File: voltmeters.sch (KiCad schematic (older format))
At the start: 27 parts

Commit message: - added DC/DC converter to library, - moved ammeter & drivers to sub-sheet, - further develop
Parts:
- R?: value 10M -> 500M
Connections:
- net U_Wh renamed U_Ext
- net U_adcWh renamed U_adcExt
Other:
- note added: "I_drawn = U_meas/R_in"
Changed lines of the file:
@@
 $Descr A4 11693 8268
 encoding utf-8
-Sheet 7 7
+Sheet 7 8
 Title ""
 Date ""
@@
 AR Path="/5F479892/5F479BF7" Ref="R?"  Part="1"
 F 0 "R?" V 4500 2350 50  0000 C CNN
-F 1 "10M" V 4300 2350 50  0000 C CNN
+F 1 "500M" V 4300 2350 50  0000 C CNN
 F 2 "" V 4330 2350 50  0001 C CNN
 F 3 "~" H 4400 2350 50  0001 C CNN
@@
 $EndComp
 Text Notes 3350 2050 0    50   ~ 0
-I_drawn = U_meas/10M
+I_drawn = U_meas/R_in
 Wire Wire Line
 	5300 2050 5300 2350
@@
 U_K
 Text HLabel 3800 4950 0    50   Input ~ 0
-U_Wh
+U_Ext
 Text HLabel 6700 1950 2    50   Output ~ 0
 U_adcFocus
@@
 U_adcK
 Text HLabel 6700 4550 2    50   Output ~ 0
-U_adcWh
+U_adcExt
 $Comp
 L Device:C_Small C?

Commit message: - added supply sch draft
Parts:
- removed R? (x2): 10M, symbol Device:R
- added R? (x2): 500M, symbol Device:R
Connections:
- net U_Ext: now also R?.1
- net U_K: now also R?.1
- net at C?.2, R?.1, U?.2 (-): now also R?.2 (x2)
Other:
- note removed: "I_drawn = U_meas/10M"
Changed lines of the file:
@@
 $Descr A4 11693 8268
 encoding utf-8
-Sheet 7 8
+Sheet 6 9
 Title ""
 Date ""
@@
 $EndComp
 $Comp
-L power:GND #PWR?
-U 1 1 5F479BF1
-P 4700 1950
-AR Path="/5F40DCB9/5F479BF1" Ref="#PWR?"  Part="1"
-AR Path="/5F479892/5F479BF1" Ref="#PWR?"  Part="1"
-F 0 "#PWR?" H 4700 1790 50  0001 C CNN
-F 1 "GND" V 4700 1873 39  0000 R CNN
-F 2 "" H 4700 1950 50  0001 C CNN
-F 3 "" H 4700 1950 50  0001 C CNN
-	1    4700 1950
-	0    1    1    0
-$EndComp
-$Comp
 L Device:R R?
 U 1 1 5F479BF7
@@
 	1    6050 2350
 	0    -1   -1   0
-$EndComp
-$Comp
-L power:GND #PWR?
-U 1 1 5F479C10
-P 5800 1850
-AR Path="/5F40DCB9/5F479C10" Ref="#PWR?"  Part="1"
-AR Path="/5F479892/5F479C10" Ref="#PWR?"  Part="1"
-F 0 "#PWR?" H 5800 1690 50  0001 C CNN
-F 1 "GND" V 5800 1773 39  0000 R CNN
-F 2 "" H 5800 1850 50  0001 C CNN
-F 3 "" H 5800 1850 50  0001 C CNN
-	1    5800 1850
-	0    1    1    0
 $EndComp
 Wire Wire Line
@@
 	0    -1   -1   0
 $EndComp
-$Comp
-L power:GND #PWR?
-U 1 1 5F479C4C
-P 4700 3250
-AR Path="/5F40DCB9/5F479C4C" Ref="#PWR?"  Part="1"
-AR Path="/5F479892/5F479C4C" Ref="#PWR?"  Part="1"
-F 0 "#PWR?" H 4700 3090 50  0001 C CNN
-F 1 "GND" V 4700 3173 39  0000 R CNN
-F 2 "" H 4700 3250 50  0001 C CNN
-F 3 "" H 4700 3250 50  0001 C CNN
-	1    4700 3250
-	0    1    1    0
-$EndComp
-$Comp
-L Device:R R?
-U 1 1 5F479C52
-P 4400 3650
-AR Path="/5F40DCB9/5F479C52" Ref="R?"  Part="1"
-AR Path="/5F479892/5F479C52" Ref="R?"  Part="1"
-F 0 "R?" V 4500 3650 50  0000 C CNN
-F 1 "10M" V 4300 3650 50  0000 C CNN
-F 2 "" V 4330 3650 50  0001 C CNN
-F 3 "~" H 4400 3650 50  0001 C CNN
-	1    4400 3650
-	0    -1   -1   0
-$EndComp
 Wire Wire Line
 	4700 3450 4700 3650
@@
 	1    6050 3650
 	0    -1   -1   0
-$EndComp
-$Comp
-L power:GND #PWR?
-U 1 1 5F479C6B
-P 5800 3150
-AR Path="/5F40DCB9/5F479C6B" Ref="#PWR?"  Part="1"
-AR Path="/5F479892/5F479C6B" Ref="#PWR?"  Part="1"
-F 0 "#PWR?" H 5800 2990 50  0001 C CNN
-F 1 "GND" V 5800 3073 39  0000 R CNN
-F 2 "" H 5800 3150 50  0001 C CNN
-F 3 "" H 5800 3150 50  0001 C CNN
-	1    5800 3150
-	0    1    1    0
 $EndComp
 Wire Wire Line
@@
 	-1   0    0    1
 $EndComp
-Text Notes 3500 3350 0    50   ~ 0
-I_drawn = U_meas/10M
 Wire Wire Line
 	5300 3350 5300 3650
@@
 	0    -1   -1   0
 $EndComp
-$Comp
-L power:GND #PWR?
-U 1 1 5F479CA7
-P 4700 4550
-AR Path="/5F40DCB9/5F479CA7" Ref="#PWR?"  Part="1"
-AR Path="/5F479892/5F479CA7" Ref="#PWR?"  Part="1"
-F 0 "#PWR?" H 4700 4390 50  0001 C CNN
-F 1 "GND" V 4700 4473 39  0000 R CNN
-F 2 "" H 4700 4550 50  0001 C CNN
-F 3 "" H 4700 4550 50  0001 C CNN
-	1    4700 4550
-	0    1    1    0
-$EndComp
-$Comp
-L Device:R R?
-U 1 1 5F479CAD
-P 4400 4950
-AR Path="/5F40DCB9/5F479CAD" Ref="R?"  Part="1"
-AR Path="/5F479892/5F479CAD" Ref="R?"  Part="1"
-F 0 "R?" V 4500 4950 50  0000 C CNN
-F 1 "10M" V 4300 4950 50  0000 C CNN
-F 2 "" V 4330 4950 50  0001 C CNN
-F 3 "~" H 4400 4950 50  0001 C CNN
-	1    4400 4950
-	0    -1   -1   0
-$EndComp
 Wire Wire Line
 	4700 4750 4700 4950
@@
 	1    6050 4950
 	0    -1   -1   0
-$EndComp
-$Comp
-L power:GND #PWR?
-U 1 1 5F479CC6
-P 5800 4450
-AR Path="/5F40DCB9/5F479CC6" Ref="#PWR?"  Part="1"
-AR Path="/5F479892/5F479CC6" Ref="#PWR?"  Part="1"
-F 0 "#PWR?" H 5800 4290 50  0001 C CNN
-F 1 "GND" V 5800 4373 39  0000 R CNN
-F 2 "" H 5800 4450 50  0001 C CNN
-F 3 "" H 5800 4450 50  0001 C CNN
-	1    5800 4450
-	0    1    1    0
 $EndComp
 Wire Wire Line
@@
 	-1   0    0    1
 $EndComp
-Text Notes 3450 4600 0    50   ~ 0
-I_drawn = U_meas/10M
 Wire Wire Line
 	5300 4650 5300 4950
@@
 Wire Wire Line
 	6400 5200 6400 4950
+$Comp
+L power:GND #PWR?
+U 1 1 5F62A73A
+P 4700 1950
+AR Path="/5F40DCB9/5F62A73A" Ref="#PWR?"  Part="1"
+AR Path="/5F618AB9/5F62A73A" Ref="#PWR?"  Part="1"
+AR Path="/5F62A73A" Ref="#PWR?"  Part="1"
+AR Path="/5F479892/5F62A73A" Ref="#PWR?"  Part="1"
+F 0 "#PWR?" H 4700 1790 50  0001 C CNN
+F 1 "GND" V 4700 1850 39  0000 R CNN
+F 2 "" H 4700 1950 50  0001 C CNN
+F 3 "" H 4700 1950 50  0001 C CNN
+	1    4700 1950
+	0    1    1    0
+$EndComp
+$Comp
+L power:GND #PWR?
+U 1 1 5F62B7FF
+P 5800 1850
+AR Path="/5F40DCB9/5F62B7FF" Ref="#PWR?"  Part="1"
+AR Path="/5F618AB9/5F62B7FF" Ref="#PWR?"  Part="1"
+AR Path="/5F62B7FF" Ref="#PWR?"  Part="1"
+AR Path="/5F479892/5F62B7FF" Ref="#PWR?"  Part="1"
+F 0 "#PWR?" H 5800 1690 50  0001 C CNN
+F 1 "GND" V 5800 1750 39  0000 R CNN
+F 2 "" H 5800 1850 50  0001 C CNN
+F 3 "" H 5800 1850 50  0001 C CNN
+	1    5800 1850
+	0    1    1    0
+$EndComp
+$Comp
+L power:GND #PWR?
+U 1 1 5F62C9BB
+P 4700 3250
+AR Path="/5F40DCB9/5F62C9BB" Ref="#PWR?"  Part="1"
+AR Path="/5F618AB9/5F62C9BB" Ref="#PWR?"  Part="1"
+AR Path="/5F62C9BB" Ref="#PWR?"  Part="1"
+AR Path="/5F479892/5F62C9BB" Ref="#PWR?"  Part="1"
+F 0 "#PWR?" H 4700 3090 50  0001 C CNN
+F 1 "GND" V 4700 3150 39  0000 R CNN
+F 2 "" H 4700 3250 50  0001 C CNN
+F 3 "" H 4700 3250 50  0001 C CNN
+	1    4700 3250
+	0    1    1    0
+$EndComp
+$Comp
+L power:GND #PWR?
+U 1 1 5F62DA80
+P 5800 3150
+AR Path="/5F40DCB9/5F62DA80" Ref="#PWR?"  Part="1"
+AR Path="/5F618AB9/5F62DA80" Ref="#PWR?"  Part="1"
+AR Path="/5F62DA80" Ref="#PWR?"  Part="1"
+AR Path="/5F479892/5F62DA80" Ref="#PWR?"  Part="1"
+F 0 "#PWR?" H 5800 2990 50  0001 C CNN
+F 1 "GND" V 5800 3050 39  0000 R CNN
+F 2 "" H 5800 3150 50  0001 C CNN
+F 3 "" H 5800 3150 50  0001 C CNN
+	1    5800 3150
+	0    1    1    0
+$EndComp
+$Comp
+L power:GND #PWR?
+U 1 1 5F62EB45
+P 5800 4450
+AR Path="/5F40DCB9/5F62EB45" Ref="#PWR?"  Part="1"
+AR Path="/5F618AB9/5F62EB45" Ref="#PWR?"  Part="1"
+AR Path="/5F62EB45" Ref="#PWR?"  Part="1"
+AR Path="/5F479892/5F62EB45" Ref="#PWR?"  Part="1"
+F 0 "#PWR?" H 5800 4290 50  0001 C CNN
+F 1 "GND" V 5800 4350 39  0000 R CNN
+F 2 "" H 5800 4450 50  0001 C CNN
+F 3 "" H 5800 4450 50  0001 C CNN
+	1    5800 4450
+	0    1    1    0
+$EndComp
+$Comp
+L power:GND #PWR?
+U 1 1 5F62FC0A
+P 4700 4550
+AR Path="/5F40DCB9/5F62FC0A" Ref="#PWR?"  Part="1"
+AR Path="/5F618AB9/5F62FC0A" Ref="#PWR?"  Part="1"
+AR Path="/5F62FC0A" Ref="#PWR?"  Part="1"
+AR Path="/5F479892/5F62FC0A" Ref="#PWR?"  Part="1"
+F 0 "#PWR?" H 4700 4390 50  0001 C CNN
+F 1 "GND" V 4700 4450 39  0000 R CNN
+F 2 "" H 4700 4550 50  0001 C CNN
+F 3 "" H 4700 4550 50  0001 C CNN
+	1    4700 4550
+	0    1    1    0
+$EndComp
+$Comp
+L Device:R R?
+U 1 1 5F631A1F
+P 4400 3650
+AR Path="/5F40DCB9/5F631A1F" Ref="R?"  Part="1"
+AR Path="/5F479892/5F631A1F" Ref="R?"  Part="1"
+F 0 "R?" V 4500 3650 50  0000 C CNN
+F 1 "500M" V 4300 3650 50  0000 C CNN
+F 2 "" V 4330 3650 50  0001 C CNN
+F 3 "~" H 4400 3650 50  0001 C CNN
+	1    4400 3650
+	0    -1   -1   0
+$EndComp
+$Comp
+L Device:R R?
+U 1 1 5F631ACB
+P 4400 4950
+AR Path="/5F40DCB9/5F631ACB" Ref="R?"  Part="1"
+AR Path="/5F479892/5F631ACB" Ref="R?"  Part="1"
+F 0 "R?" V 4500 4950 50  0000 C CNN
+F 1 "500M" V 4300 4950 50  0000 C CNN
+F 2 "" V 4330 4950 50  0001 C CNN
+F 3 "~" H 4400 4950 50  0001 C CNN
+	1    4400 4950
+	0    -1   -1   0
+$EndComp
 $EndSCHEMATC

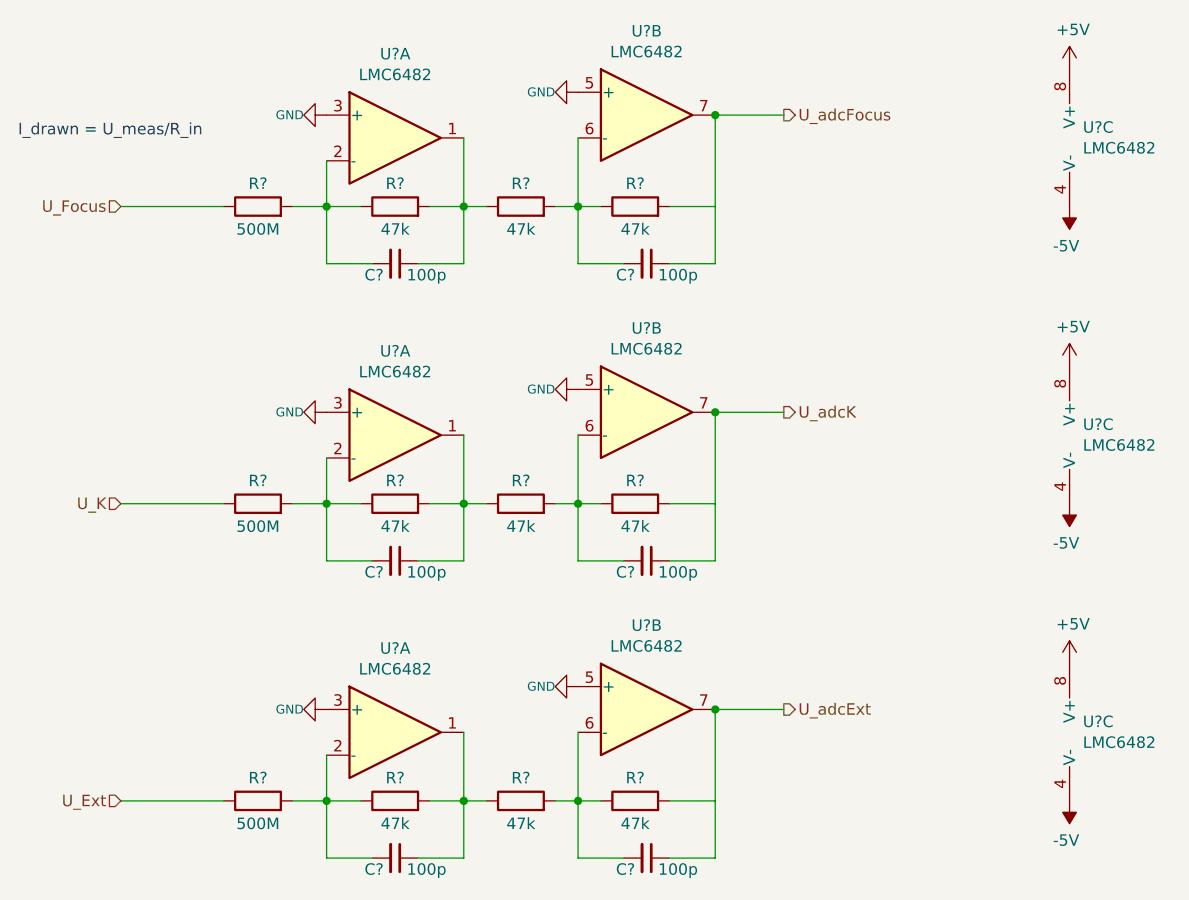
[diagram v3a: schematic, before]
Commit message: - supply converter develop - added sheet: MCU - cleanup 'koncepcja' sub-schematics
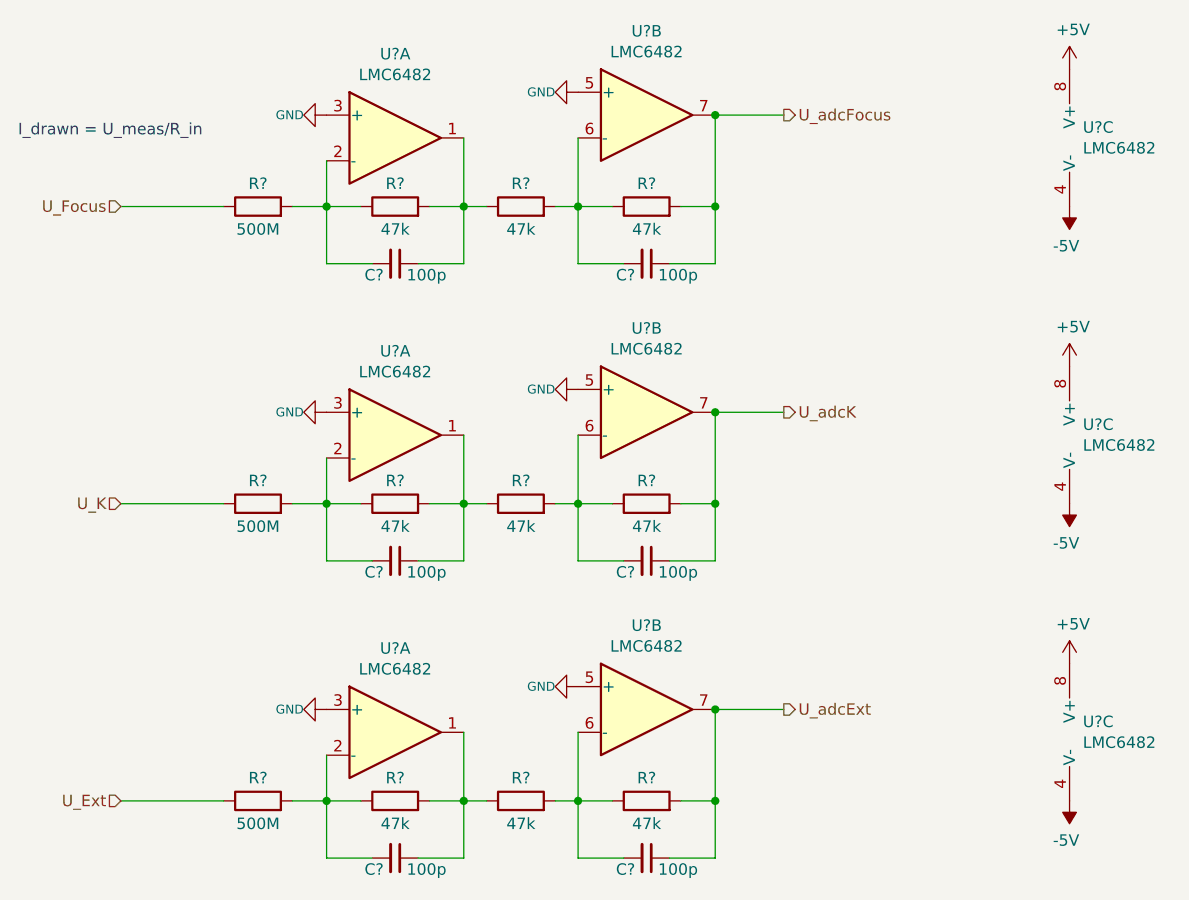
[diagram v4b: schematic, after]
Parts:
- removed C? (x5): 100p, symbol Device:C_Small
- removed R? (x8): 47k, symbol Device:R
- added C? (x5): 100p, Capacitor_SMD:C_0805_2012Metric_Pad1.15x1.40mm_HandSolder, symbol Device:C_Small
- added R? (x8): 47k, Resistor_SMD:R_0603_1608Metric_Pad1.05x0.95mm_HandSolder, symbol Device:R
- C?: footprint (none) -> Capacitor_SMD:C_0805_2012Metric_Pad1.15x1.40mm_HandSolder
- R?: footprint (none) -> Resistor_SMD:R_0603_1608Metric_Pad1.05x0.95mm_HandSolder
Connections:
- net U_adcExt: now also C?.1
- net U_adcFocus: now also C?.1, R?.2
- net U_adcK: now also C?.1, R?.2
- net at C?.1, U?.1: now also R?.1, R?.2
- net at C?.2, R?.2, U?.2 (-): now also R?.1
- net at U?.6 (-): now also C?.2, R?.1, R?.2 (x2)
- net at U?.1: now also C?.1, R?.1, R?.2 (x2)
- net at R?.2, U?.2 (-): now also C?.2, R?.1 (x2)
- net at R?.1, U?.6 (-): now also C?.2, R?.2
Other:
- moved on the sheet: R?

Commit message: - added footprint & 3D model of DC/DC HV converter - updated battery (to 2x battery holder) - some changes in supply
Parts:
- removed R? (x2): 500M, symbol Device:R
- added R? (x2): 500M, resistors_moje:MHR0317SA, symbol Device:R
- R?: footprint (none) -> resistors_moje:MHR0317SA
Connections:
- net U_Ext: now also R?.1
- net U_K: now also R?.1
- net at C?.2, R?.1, U?.2 (-): now also R?.2 (x2)
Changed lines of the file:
@@
 $Descr A4 11693 8268
 encoding utf-8
-Sheet 6 9
+Sheet 4 9
 Title ""
 Date ""
@@
 F 0 "R?" V 4500 2350 50  0000 C CNN
 F 1 "500M" V 4300 2350 50  0000 C CNN
-F 2 "" V 4330 2350 50  0001 C CNN
+F 2 "resistors_moje:MHR0317SA" V 4330 2350 50  0001 C CNN
 F 3 "~" H 4400 2350 50  0001 C CNN
 	1    4400 2350
@@
 $EndComp
 $Comp
-L Device:R R?
-U 1 1 5F631A1F
-P 4400 3650
-AR Path="/5F40DCB9/5F631A1F" Ref="R?"  Part="1"
-AR Path="/5F479892/5F631A1F" Ref="R?"  Part="1"
-F 0 "R?" V 4500 3650 50  0000 C CNN
-F 1 "500M" V 4300 3650 50  0000 C CNN
-F 2 "" V 4330 3650 50  0001 C CNN
-F 3 "~" H 4400 3650 50  0001 C CNN
-	1    4400 3650
-	0    -1   -1   0
-$EndComp
-$Comp
-L Device:R R?
-U 1 1 5F631ACB
-P 4400 4950
-AR Path="/5F40DCB9/5F631ACB" Ref="R?"  Part="1"
-AR Path="/5F479892/5F631ACB" Ref="R?"  Part="1"
-F 0 "R?" V 4500 4950 50  0000 C CNN
-F 1 "500M" V 4300 4950 50  0000 C CNN
-F 2 "" V 4330 4950 50  0001 C CNN
-F 3 "~" H 4400 4950 50  0001 C CNN
-	1    4400 4950
-	0    -1   -1   0
-$EndComp
-$Comp
 L Device:C_Small C?
 U 1 1 5F8ED95A
@@
 	0    -1   -1   0
 $EndComp
+$Comp
+L Device:R R?
+U 1 1 5F6E8D99
+P 4400 3650
+AR Path="/5F40DCB9/5F6E8D99" Ref="R?"  Part="1"
+AR Path="/5F479892/5F6E8D99" Ref="R?"  Part="1"
+F 0 "R?" V 4500 3650 50  0000 C CNN
+F 1 "500M" V 4300 3650 50  0000 C CNN
+F 2 "resistors_moje:MHR0317SA" V 4330 3650 50  0001 C CNN
+F 3 "~" H 4400 3650 50  0001 C CNN
+	1    4400 3650
+	0    -1   -1   0
+$EndComp
+$Comp
+L Device:R R?
+U 1 1 5F6E8E1F
+P 4400 4950
+AR Path="/5F40DCB9/5F6E8E1F" Ref="R?"  Part="1"
+AR Path="/5F479892/5F6E8E1F" Ref="R?"  Part="1"
+F 0 "R?" V 4500 4950 50  0000 C CNN
+F 1 "500M" V 4300 4950 50  0000 C CNN
+F 2 "resistors_moje:MHR0317SA" V 4330 4950 50  0001 C CNN
+F 3 "~" H 4400 4950 50  0001 C CNN
+	1    4400 4950
+	0    -1   -1   0
+$EndComp

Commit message: - W.i.P.
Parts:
- removed R? (x8): 47k, Resistor_SMD:R_0603_1608Metric_Pad1.05x0.95mm_HandSolder, symbol Device:R
- removed R? (x2): 500M, resistors_moje:MHR0317SA, symbol Device:R
- added R? (x2): 500M, resistors_moje:MHR0317SA, symbol Device:R
- added R? (x8): 47k, Resistor_SMD:R_0603_1608Metric_Pad1.05x0.95mm_HandSolder, symbol Device:R_Small
- R?: Mfr. (none) -> Murata; Mfr. No: (none) -> MHR0317SA507F70; Price [PLN] (none) -> 1.34
- R?: symbol Device:R -> Device:R_Small
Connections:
- net U_Ext: now also R?.1
- net U_K: now also R?.1
- net U_adcExt: now also R?.2
- net U_adcFocus: now also R?.2
- net U_adcK: now also R?.2
- net at C?.1, R?.2, U?.1: now also R?.1
- net at C?.2, U?.6 (-): now also R?.1, R?.2 (x3)
- net at C?.1, U?.1: now also R?.1, R?.2 (x2)
- net at C?.2, U?.2 (-): now also R?.1, R?.2 (x2)

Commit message: - drivers modified - MCU replaced
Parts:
- R? (x3): footprint resistors_moje:MHR0317SA -> resistors_moje:MHR0317_0422_0424_0624SA
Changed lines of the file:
@@
 F 0 "R?" V 4500 2350 50  0000 C CNN
 F 1 "500M" V 4300 2350 50  0000 C CNN
-F 2 "resistors_moje:MHR0317SA" V 4330 2350 50  0001 C CNN
+F 2 "resistors_moje:MHR0317_0422_0424_0624SA" V 4330 2350 50  0001 C CNN
 F 3 "~" H 4400 2350 50  0001 C CNN
 F 4 "MHR0317SA507F70" V 4400 2350 50  0001 C CNN "Mfr. No:"
@@
 F 0 "R?" V 4500 3650 50  0000 C CNN
 F 1 "500M" V 4300 3650 50  0000 C CNN
-F 2 "resistors_moje:MHR0317SA" V 4330 3650 50  0001 C CNN
+F 2 "resistors_moje:MHR0317_0422_0424_0624SA" V 4330 3650 50  0001 C CNN
 F 3 "~" H 4400 3650 50  0001 C CNN
 F 4 "MHR0317SA507F70" V 4400 3650 50  0001 C CNN "Mfr. No:"
@@
 F 0 "R?" V 4500 4950 50  0000 C CNN
 F 1 "500M" V 4300 4950 50  0000 C CNN
-F 2 "resistors_moje:MHR0317SA" V 4330 4950 50  0001 C CNN
+F 2 "resistors_moje:MHR0317_0422_0424_0624SA" V 4330 4950 50  0001 C CNN
 F 3 "~" H 4400 4950 50  0001 C CNN
 F 4 "MHR0317SA507F70" V 4400 4950 50  0001 C CNN "Mfr. No:"
